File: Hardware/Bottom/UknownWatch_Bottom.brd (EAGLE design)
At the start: 33 x 33 mm, 32 parts, among them U1 AD5242-SO16

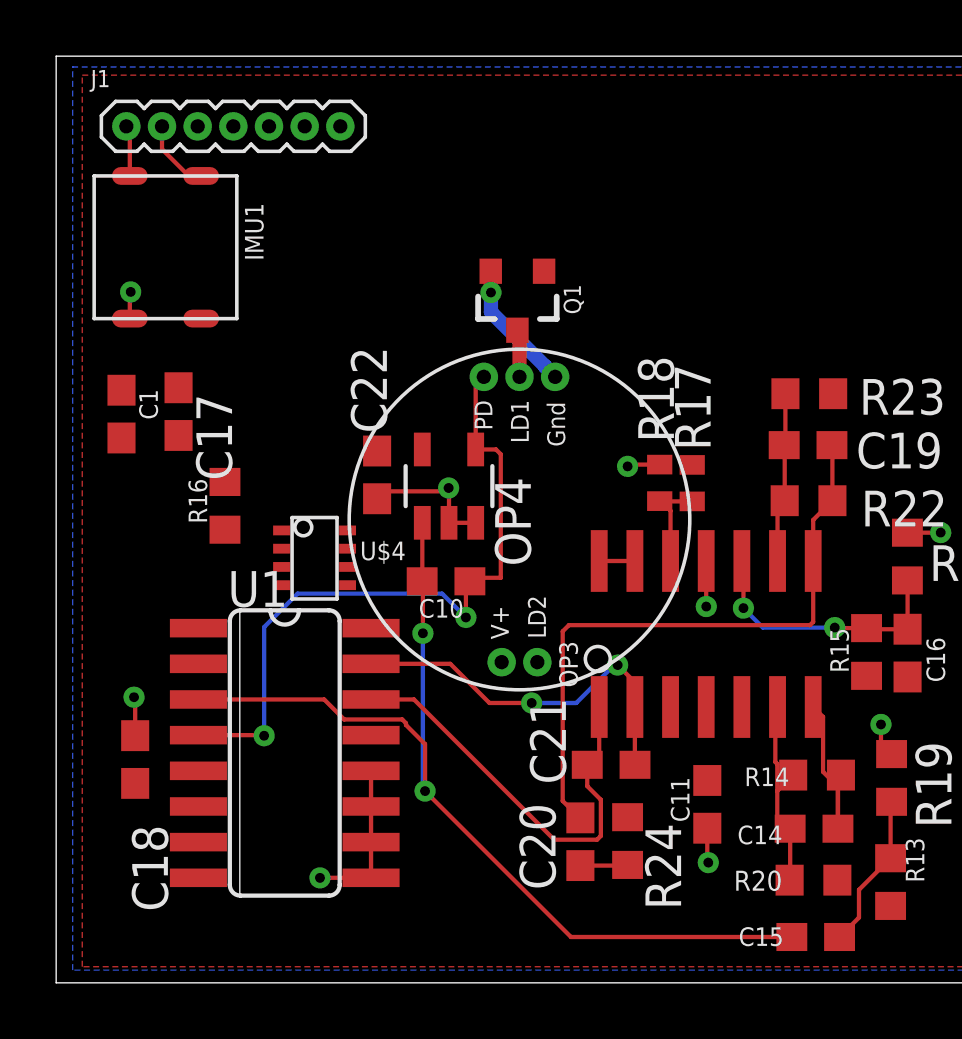
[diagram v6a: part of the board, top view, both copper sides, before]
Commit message: Routed more of bottom board
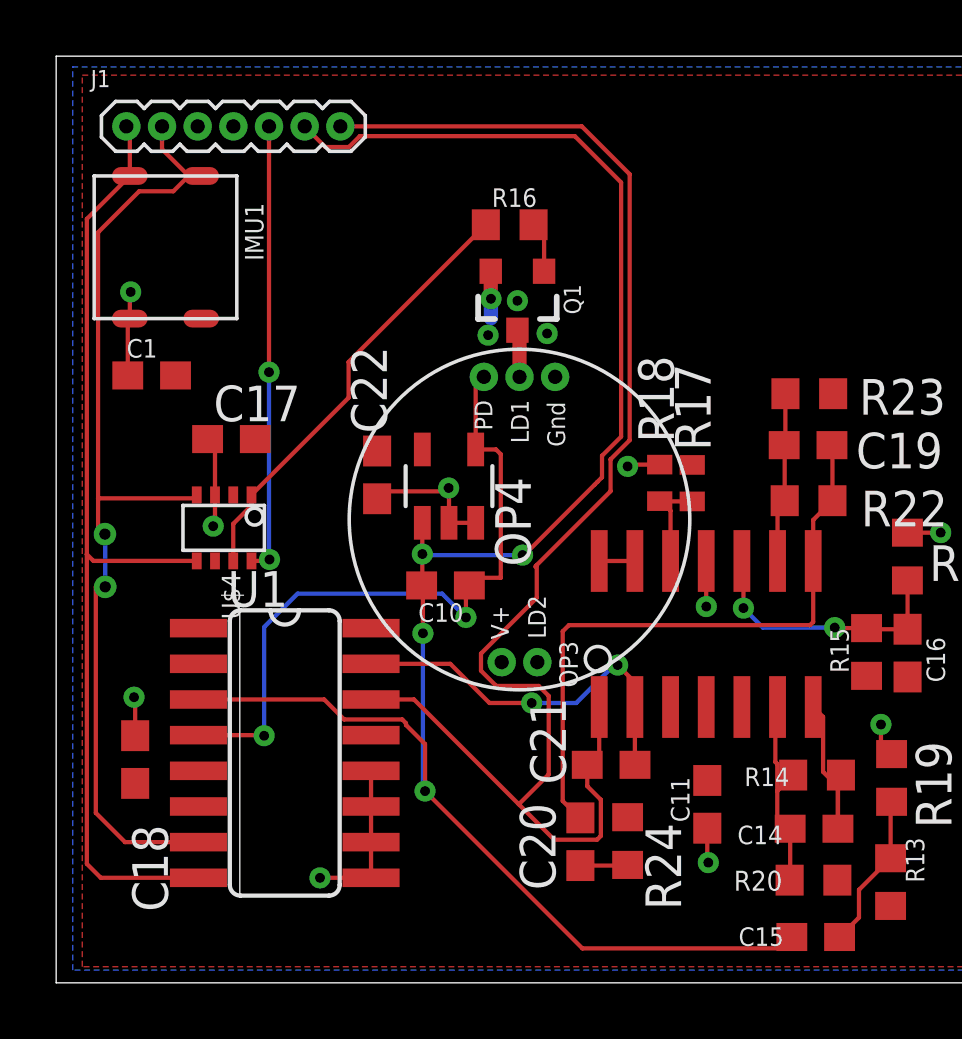
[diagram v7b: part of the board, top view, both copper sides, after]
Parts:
- moved R16 14.2 mm to (18.7, 29.5), turned to 0 degrees
- moved U$4 3.41 mm to (8.47, 18.7), turned to 180 degrees
- moved C17 2.12 mm to (8.74, 21.9), turned to 0 degrees
- moved C1 1.75 mm to (5.90, 24.1), turned to 0 degrees
- moved C10 0.15 mm to (16.4, 16.7)
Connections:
- net A6/TIA: now also J1.6; no longer J1.5
- net D29/LED.CTRL: now also J1.5; no longer J1.6
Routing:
- net A7/PPG: track 15.9 -> 53.9 mm
- net SDA: track 1.82 -> 35.2 mm
- net SCL: track 2.60 -> 35.9 mm, vias 0 -> 2
- net A6/TIA: track 35.3 -> 66.4 mm, vias 2 -> 4
- net D29/LED.CTRL: track 0.00 -> 16.1 mm, vias 0 -> 2
- net N$9: track 0.00 -> 15.7 mm
- net GND: track 24.0 -> 26.2 mm, vias 10 -> 14
- net N$8: track 0.00 -> 1.81 mm

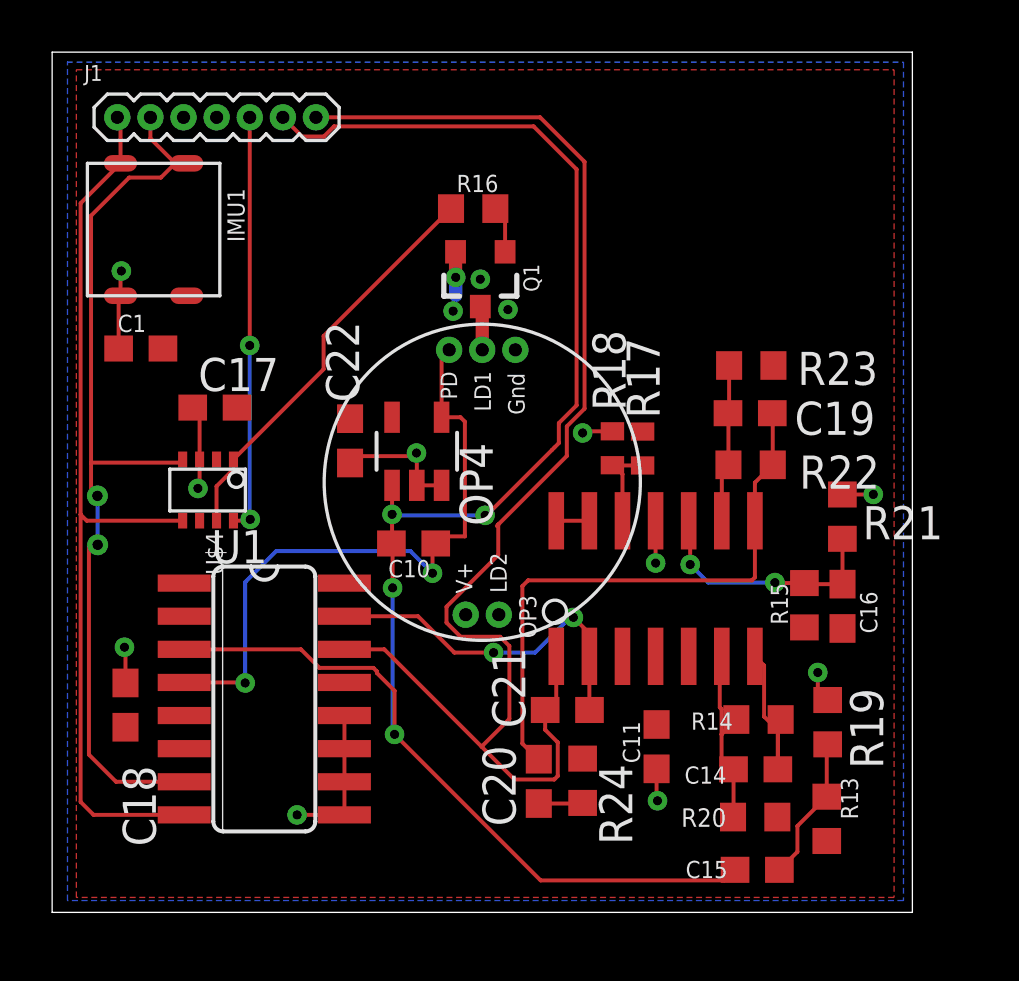
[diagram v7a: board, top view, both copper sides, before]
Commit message: Finished bulk of routing on bottom board
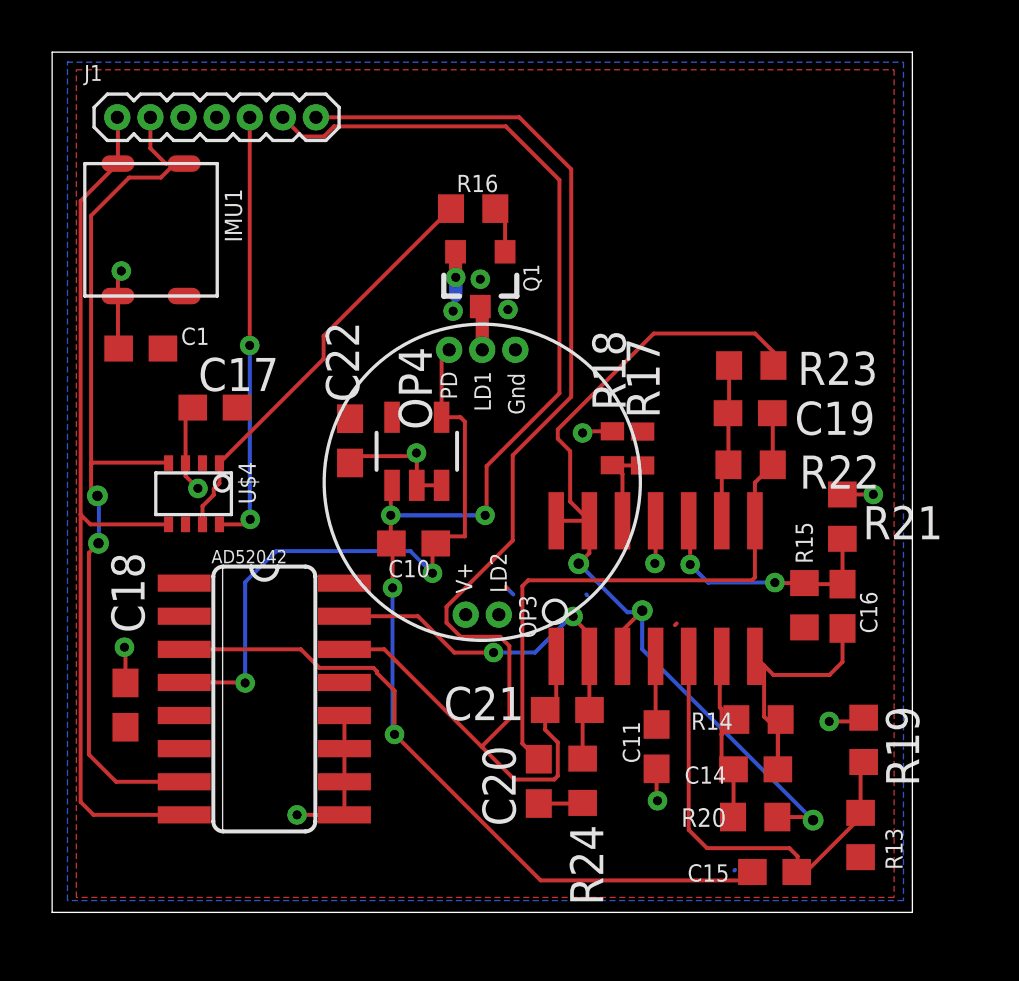
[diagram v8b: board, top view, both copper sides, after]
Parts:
- moved R19 1.54 mm to (33.6, 9.12)
- moved R13 1.44 mm to (33.5, 5.47)
- moved C15 0.67 mm to (30.2, 4.05)
- moved U$4 0.56 mm to (7.93, 18.6)
- moved IMU1 0.10 mm to (6.29, 28.7)
- renumbered U1 to AD52042
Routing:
- net VREF: track 1.27 -> 34.3 mm, vias 0 -> 3
- net N$13: track 5.58 -> 17.8 mm
- net N$16: track 6.65 -> 11.3 mm
- net 3.3V: track 0.00 -> 3.27 mm
- net G.W2: track 12.9 -> 14.9 mm
- net A7/PPG: track 53.9 -> 52.4 mm
- net SCL: track 35.9 -> 35.2 mm
- net SDA: track 35.2 -> 34.6 mm
- net D29/LED.CTRL: track 16.1 -> 16.7 mm
